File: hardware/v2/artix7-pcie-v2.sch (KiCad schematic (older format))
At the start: 14 parts, among them J1 JTAG, J2 JTAG_EN, SW1 PROG, U1 XC7A75T-FGG484, U2 W25Q64JVSSIM

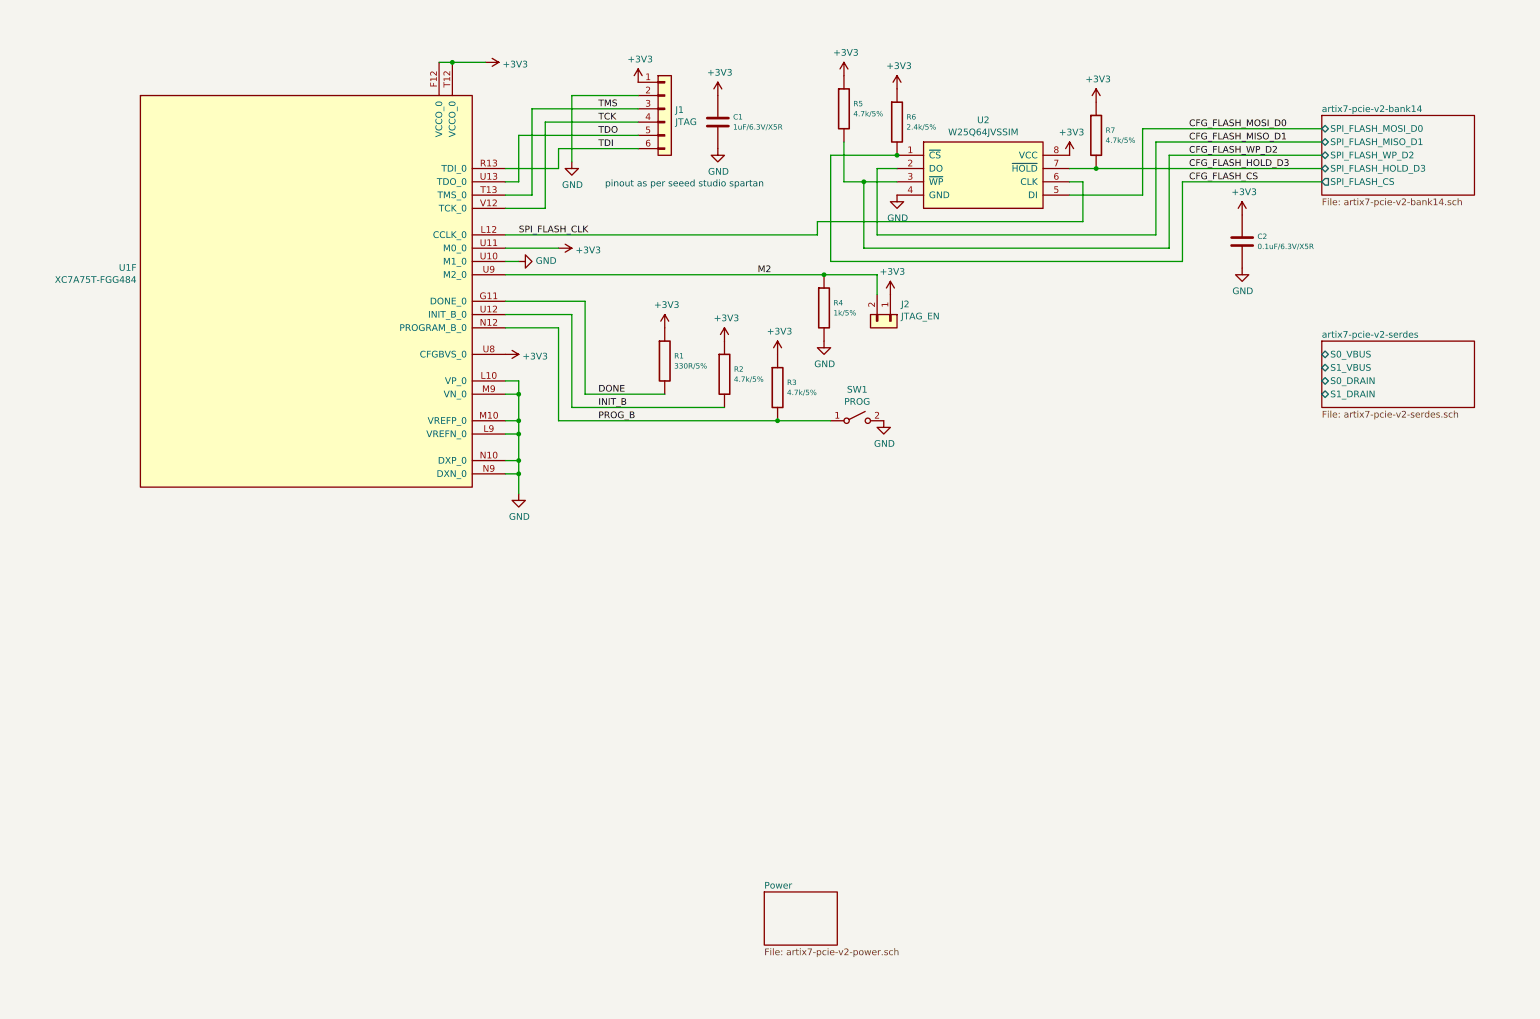
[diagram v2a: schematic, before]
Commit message: v2 hardware - all io connectors in schematic
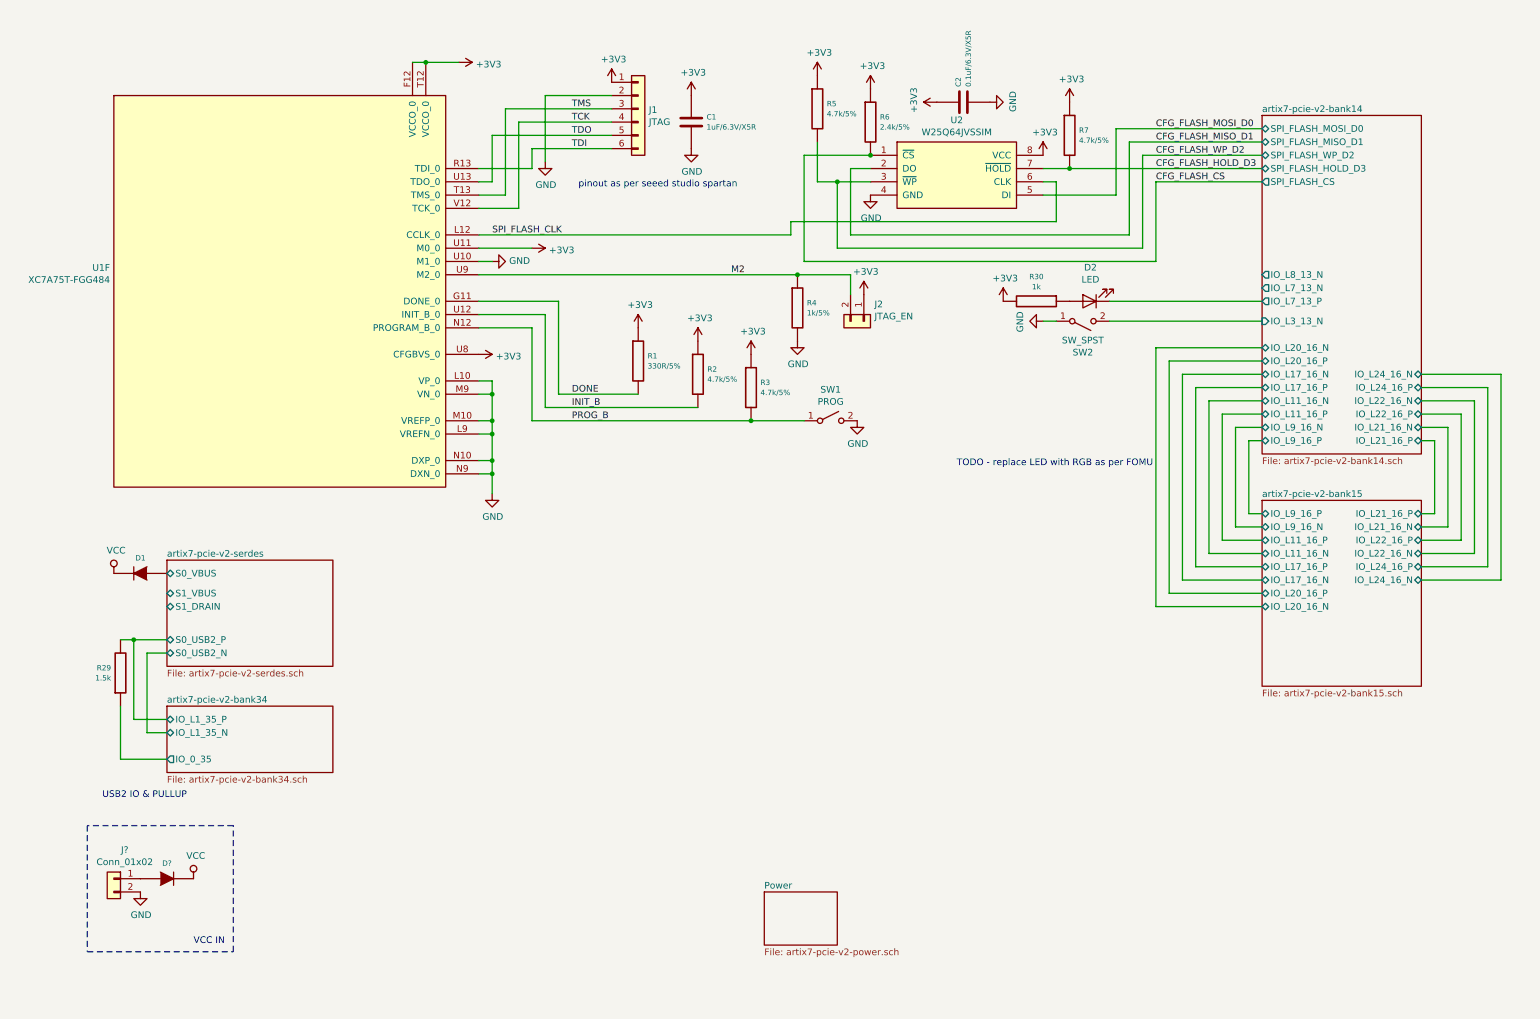
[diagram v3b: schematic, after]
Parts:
- added D1, D?: SBR3U20SA-13‎, tom-semiconductors:D_SMA, symbol tom-passives:DIODE
- added D2: LED, tom-passives:C_0402_1005Metric, symbol tom-opto:LED
- added J?: Conn_01x02, symbol tom-connectors:Conn_01x02
- added R29: 1.5k, tom-passives:C_0402_1005Metric, symbol tom-passives:R
- added R30: 1k, tom-passives:C_0402_1005Metric, symbol tom-passives:R
- added SW2: SW_SPST, tom-mechanical:SW_Push_1P1T_NO_CK_KMR2, symbol tom-mechanical:SW_SPST
- J1: footprint (none) -> tom-connectors:PinHeader_1x06_P2.54mm_Vertical_SMD_Pin1Left
- J2: footprint (none) -> tom-connectors:PinHeader_1x02_P1.27mm_Vertical
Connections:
- net +3V3: now also R30.2
- net GND: now also J?.2 (Pin_2), SW2.1 (A)
- net artix7-pcie-v2-serdes/S0_VBUS: now also D1.1 (A)
- new net: D2.2 (A), R30.1
- new net: D?.1 (A), J?.1 (Pin_1)
- new net VCC: D1.2 (K), D?.2 (K)
- new net artix7-pcie-v2-bank14/IO_L3_13_N: SW2.2 (B)
- new net artix7-pcie-v2-bank14/IO_L7_13_P: D2.1 (K)
- new net artix7-pcie-v2-bank34/IO_0_35: R29.1
- new net artix7-pcie-v2-bank34/IO_L1_35_P: R29.2
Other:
- note added: "TODO - replace LED with RGB as per FOMU"
- note added: "USB2 IO & PULLUP"
- note added: "VCC IN"
- moved on the sheet: C1, C2, J1, J2, R1, R2, R3, R4, R5, R6, R7, SW1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

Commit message: v2 schematic/pcb: band 13 to NC for smaller device compatibility
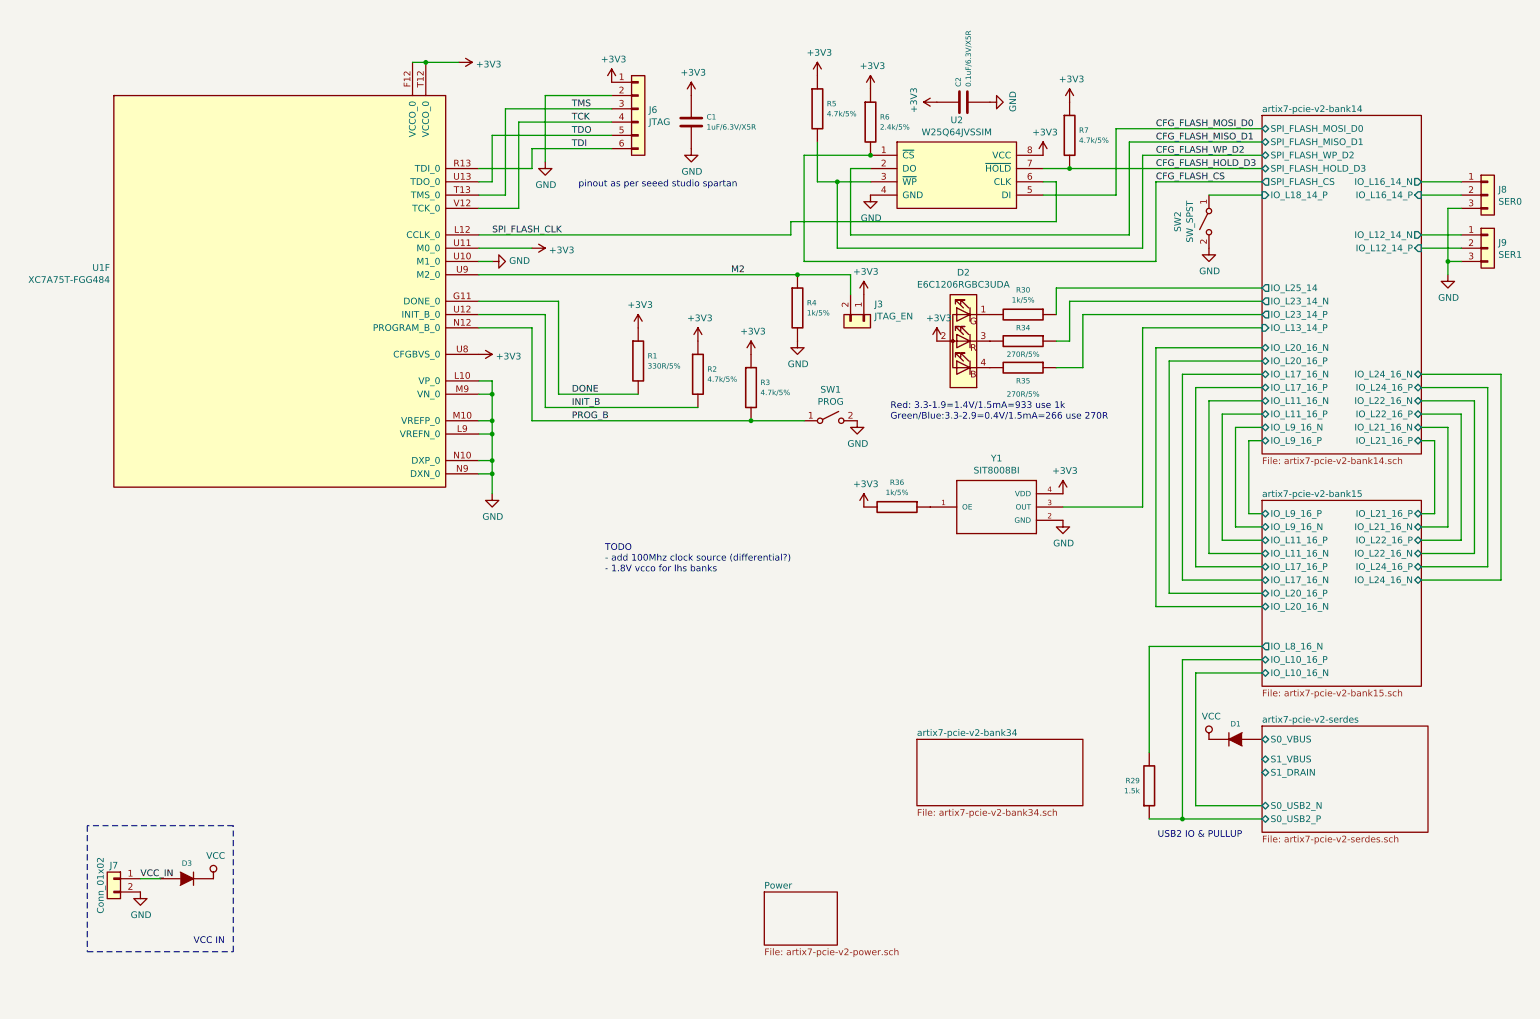
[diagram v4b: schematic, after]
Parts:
- removed D2: LED, tom-passives:C_0402_1005Metric, symbol tom-opto:LED
- added D2: E6C1206RGBC3UDA, tom-opto:E6C1206RGBC3UDA, symbol tom-opto:E6C1206RGBC3UDA
- added J8: SER0, tom-connectors:PinHeader_1x03_P2.54mm_Vertical, symbol tom-connectors:Conn_01x03
- added J9: SER1, tom-connectors:PinHeader_1x03_P2.54mm_Vertical, symbol tom-connectors:Conn_01x03
- added R34, R35: 270R/5%, tom-passives:C_0402_1005Metric, symbol tom-passives:R
- added R36: 1k/5%, tom-passives:C_0402_1005Metric, symbol tom-passives:R
- added Y1: SIT8008BI, tom-modules:OSC_SIT8008BI, symbol tom-modules:SIT8008BI
- J7: renamed from J?; footprint (none) -> tom-connectors:JST-2-SMD
- R30: value 1k -> 1k/5%
- gave numbers to parts that had none: 1
- renumbered J2 to J3, J1 to J6
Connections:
- net artix7-pcie-v2-bank14/IO_L3_13_N is gone; now on net GND: SW2.2 (B)
- net +3V3: now also D2.2 (A), R36.2, Y1.4 (VDD); no longer R30.2
- net GND: now also J8.3 (Pin_3), J9.3 (Pin_3), Y1.2 (GND); no longer SW2.1 (A)
- net artix7-pcie-v2-bank14/IO_L25_14: now reaches R30.1
- net VCC_IN: now reaches D3.1 (A), J7.1 (Pin_1)
- net artix7-pcie-v2-bank34/IO_0_35 renamed artix7-pcie-v2-bank15/IO_L10_16_P
- net artix7-pcie-v2-bank34/IO_L1_35_P renamed artix7-pcie-v2-bank15/IO_L8_16_N
- new net: D2.1 (G), R30.2
- new net: D2.3 (R), R34.2
- new net: D2.4 (B), R35.2
- new net: R36.1, Y1.1 (OE)
- new net artix7-pcie-v2-bank14/IO_L12_14_N: J9.1 (Pin_1)
- new net artix7-pcie-v2-bank14/IO_L12_14_P: J9.2 (Pin_2)
- new net artix7-pcie-v2-bank14/IO_L13_14_P: Y1.3 (OUT)
- new net artix7-pcie-v2-bank14/IO_L16_14_N: J8.1 (Pin_1)
- new net artix7-pcie-v2-bank14/IO_L16_14_P: J8.2 (Pin_2)
- new net artix7-pcie-v2-bank14/IO_L18_14_P: SW2.1 (A)
- new net artix7-pcie-v2-bank14/IO_L23_14_N: R34.1
- new net artix7-pcie-v2-bank14/IO_L23_14_P: R35.1
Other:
- note added: "Red: 3.3-1.9=1.4V/1.5mA=933 use 1k\nGreen/Blue:3.3-2.9=0.4V/1.5mA=266 use 270R"
- note added: "TODO \n- add 100Mhz clock source (differential?)\n- 1.8V vcco for lhs banks"
- note removed: "TODO - replace LED with RGB as per FOMU"
- moved on the sheet: D1, D3, R29, R30, SW2

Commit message: v2 hardware progress checkin, just prior to replacing p/s with TI parts
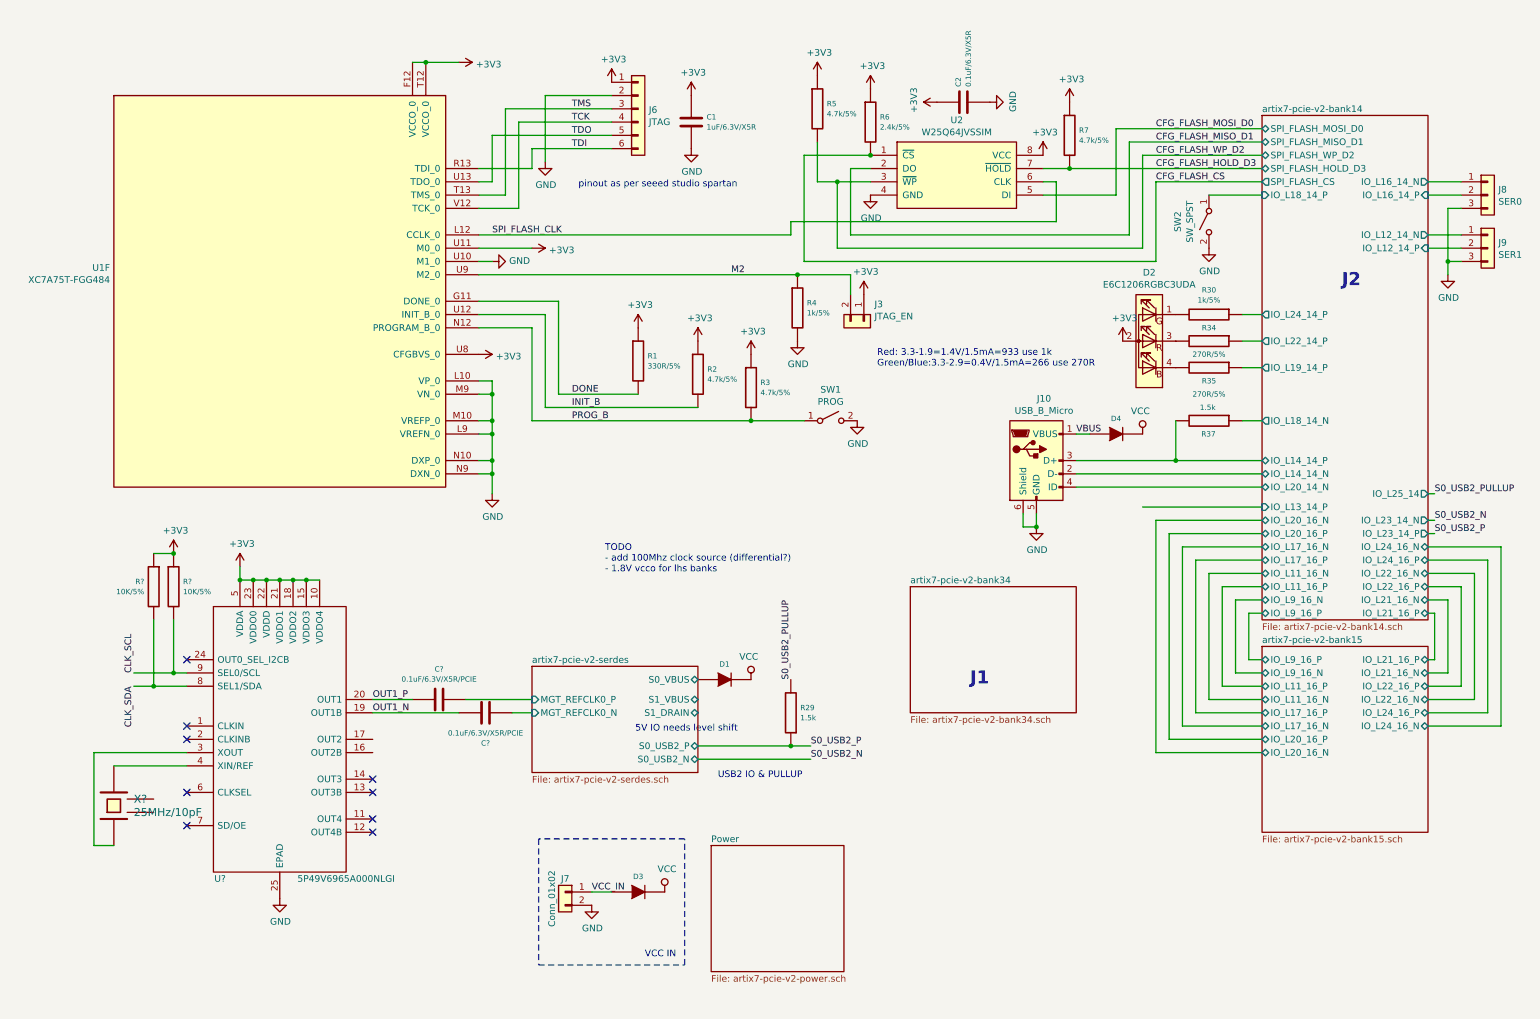
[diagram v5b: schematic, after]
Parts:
- removed R36: 1k/5%, tom-passives:C_0402_1005Metric, symbol tom-passives:R
- removed Y1: SIT8008BI, tom-modules:OSC_SIT8008BI, symbol tom-modules:SIT8008BI
- added C? (x2): 0.1uF/6.3V/X5R/PCIE, tom-passives:C_0402_1005Metric, symbol tom-passives:C
- added D4: SBR3U20SA-13‎, tom-semiconductors:D_SMA, symbol tom-passives:DIODE
- added J10: USB_B_Micro, tom-connectors:USB_MICRO_TAOBAO_SMD_PTH, symbol tom-connectors:USB_B_Micro
- added R37: 1.5k, tom-passives:C_0402_1005Metric, symbol tom-passives:R
- added R? (x2): 10K/5%, tom-passives:C_0402_1005Metric, symbol tom-passives:R
- added U?: 5P49V6965A000NLGI, QFN50P400X400X100-25N-D, symbol artix7-pcie-v2:5P49V6965A000NLGI
- added X?: 25MHz/10pF, tom-passives:Crystal_SMD_3225-4Pin_3.2x2.5mm, symbol tom-passives:CRYSTAL_4PIN
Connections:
- net +3V3: now also R?.1, R?.1, U?.10 (VDDO4), U?.15 (VDDO3), U?.18 (VDDO2), U?.21 (VDDO1), U?.22 (VDDD), U?.23 (VDDO0), U?.5 (VDDA)
- net GND: now also J10.5 (GND), J10.6 (Shield), U?.25 (EPAD)
- net VCC: now also D4.2 (K)
- net artix7-pcie-v2-bank14/IO_L23_14_N renamed artix7-pcie-v2-bank14/IO_L22_14_P
- net artix7-pcie-v2-bank14/IO_L23_14_P renamed artix7-pcie-v2-bank14/IO_L19_14_P
- net artix7-pcie-v2-bank14/IO_L25_14 renamed artix7-pcie-v2-bank14/IO_L24_14_P
- net artix7-pcie-v2-bank15/IO_L10_16_P renamed S0_USB2_P
- net artix7-pcie-v2-bank15/IO_L8_16_N renamed S0_USB2_PULLUP
- new net: U?.3 (XOUT), X?.1
- new net: U?.4 (XIN/REF), X?.3
- new net CLK_SCL: R?.2, U?.9 (SEL0/SCL)
- new net CLK_SDA: R?.2, U?.8 (SEL1/SDA)
- new net OUT1_N: C?.1, U?.19 (OUT1B)
- new net OUT1_P: C?.2, U?.20 (OUT1)
- new net VBUS: D4.1 (A), J10.1 (VBUS)
- new net artix7-pcie-v2-bank14/IO_L14_14_N: J10.2 (D-)
- new net artix7-pcie-v2-bank14/IO_L14_14_P: J10.3 (D+), R37.2
- new net artix7-pcie-v2-bank14/IO_L18_14_N: R37.1
- new net artix7-pcie-v2-bank14/IO_L20_14_N: J10.4 (ID)
- new net artix7-pcie-v2-serdes/MGT_REFCLK0_N: C?.2
- new net artix7-pcie-v2-serdes/MGT_REFCLK0_P: C?.1
- no-connect marks 0 -> 9
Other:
- note added: "5V IO needs level shift"
- note added: "J1"
- note added: "J2"
- moved on the sheet: D1, D2, D3, J7, R29, R30, R34, R35
